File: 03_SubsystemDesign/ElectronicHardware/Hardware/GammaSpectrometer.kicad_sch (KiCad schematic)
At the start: 0 parts

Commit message: pcb design work in progress
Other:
- sheet AFE ports: added +5V0_A; removed +3V3_A, -3V3_A
- sheet Analog Power ports: added +5V0_A; removed -3V3_A
- sheet FPGA IO Banks 0-1 ports: added {CLK}; removed none
- note removed: "Add Signal Domain Color Coding (Optional but pro) Some teams: Use green for power Blue for high-speed Orange for control"
- note removed: "At 65 MSPS, 12-bit parallel bus: Are you using series termination? Is FPGA bank voltage matching DRVDD? Is IO standard LVTTL 3.3 V? Is timing margin analyzed? Even if handled in sub-sheets, the system sheet should imply interface class."
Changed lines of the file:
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@@
-		)
-	)
-	(text "Add Signal Domain Color Coding (Optional but pro)\nSome teams:\n\nUse green for power\nBlue for high-speed\nOrange for control"
-		(exclude_from_sim no)
-		(at 62.23 161.29 0)
-		(effects
-			(font
-				(size 1.27 1.27)
-			)
-		)
-	)
-	(text "At 65 MSPS, 12-bit parallel bus:\n\nAre you using series termination?\nIs FPGA bank voltage matching DRVDD?\nIs IO standard LVTTL 3.3 V?\nIs timing margin analyzed?\nEven if handled in sub-sheets, the system sheet should imply interface class."
-		(exclude_from_sim no)
-		(at 83.82 76.2 0)
-		(effects
-			(font
-				(size 1.27 1.27)
-			)
 		)
 	)
@@
 	)
 	(junction
-		(at 153.67 40.64)
-		(diameter 0)
-		(color 0 0 0 0)
-	)
-	(junction
 		(at 171.45 106.68)
 		(diameter 0)
@@
 	)
 	(junction
-		(at 156.21 38.1)
+		(at 102.87 99.06)
 		(diameter 0)
 		(color 0 0 0 0)
@@
 		(color 0 0 0 0)
 	)
-	(wire
-		(pts
-			(xy 105.41 38.1) (xy 156.21 38.1)
+	(junction
+		(at 144.78 125.73)
+		(diameter 0)
+		(color 0 0 0 0)
+	)
+	(wire
+		(pts
+			(xy 105.41 38.1) (xy 194.31 38.1)
 		)
 		(stroke
@@
 	(wire
 		(pts
-			(xy 92.71 99.06) (xy 105.41 99.06)
+			(xy 92.71 99.06) (xy 102.87 99.06)
 		)
 		(stroke
@@
 		)
 	)
+	(bus
+		(pts
+			(xy 144.78 153.67) (xy 173.99 153.67)
+		)
+		(stroke
+			(width 0)
+			(type default)
+		)
+	)
 	(wire
 		(pts
@@
 	(wire
 		(pts
-			(xy 194.31 40.64) (xy 153.67 40.64)
-		)
-		(stroke
-			(width 0)
-			(type default)
-		)
-	)
-	(wire
-		(pts
 			(xy 187.96 45.72) (xy 194.31 45.72)
 		)
@@
 	(wire
 		(pts
-			(xy 194.31 38.1) (xy 156.21 38.1)
+			(xy 153.67 45.72) (xy 153.67 35.56)
+		)
+		(stroke
+			(width 0)
+			(type default)
+		)
+	)
+	(wire
+		(pts
+			(xy 102.87 40.64) (xy 102.87 99.06)
 		)
 		(stroke
@@
 		)
 	)
+	(bus
+		(pts
+			(xy 144.78 125.73) (xy 144.78 153.67)
+		)
+		(stroke
+			(width 0)
+			(type default)
+		)
+	)
+	(wire
+		(pts
+			(xy 158.75 45.72) (xy 153.67 45.72)
+		)
+		(stroke
+			(width 0)
+			(type default)
+		)
+	)
 	(wire
 		(pts
@@
 	(wire
 		(pts
-			(xy 95.25 40.64) (xy 153.67 40.64)
-		)
-		(stroke
-			(width 0)
-			(type default)
-		)
-	)
-	(wire
-		(pts
 			(xy 187.96 52.07) (xy 194.31 52.07)
 		)
@@
 	(wire
 		(pts
-			(xy 156.21 38.1) (xy 156.21 45.72)
+			(xy 194.31 40.64) (xy 102.87 40.64)
+		)
+		(stroke
+			(width 0)
+			(type default)
+		)
+	)
+	(bus
+		(pts
+			(xy 144.78 120.65) (xy 144.78 125.73)
 		)
 		(stroke
@@
 		)
 	)
-	(wire
-		(pts
-			(xy 158.75 48.26) (xy 153.67 48.26)
-		)
-		(stroke
-			(width 0)
-			(type default)
-		)
-	)
 	(bus
 		(pts
@@
 	(bus
 		(pts
+			(xy 137.16 120.65) (xy 144.78 120.65)
+		)
+		(stroke
+			(width 0)
+			(type default)
+		)
+	)
+	(bus
+		(pts
 			(xy 153.67 148.59) (xy 173.99 148.59)
 		)
@@
 	(wire
 		(pts
+			(xy 95.25 35.56) (xy 153.67 35.56)
+		)
+		(stroke
+			(width 0)
+			(type default)
+		)
+	)
+	(wire
+		(pts
 			(xy 92.71 104.14) (xy 100.33 104.14)
 		)
@@
 	(wire
 		(pts
-			(xy 156.21 45.72) (xy 158.75 45.72)
-		)
-		(stroke
-			(width 0)
-			(type default)
-		)
-	)
-	(wire
-		(pts
 			(xy 205.74 140.97) (xy 219.71 140.97)
 		)
@@
 	(wire
 		(pts
+			(xy 102.87 99.06) (xy 105.41 99.06)
+		)
+		(stroke
+			(width 0)
+			(type default)
+		)
+	)
+	(wire
+		(pts
 			(xy 171.45 99.06) (xy 214.63 99.06)
 		)
@@
 		)
 	)
+	(bus
+		(pts
+			(xy 173.99 125.73) (xy 144.78 125.73)
+		)
+		(stroke
+			(width 0)
+			(type default)
+		)
+	)
 	(wire
 		(pts
 			(xy 135.89 53.34) (xy 158.75 53.34)
-		)
-		(stroke
-			(width 0)
-			(type default)
-		)
-	)
-	(wire
-		(pts
-			(xy 153.67 40.64) (xy 153.67 48.26)
 		)
 		(stroke
@@
 	)
 	(sheet
-		(at 69.85 35.56)
+		(at 69.85 33.02)
 		(size 25.4 7.62)
 		(exclude_from_sim no)
@@
 		)
 		(property "Sheetname" "Analog Power"
-			(at 69.85 34.8484 0)
+			(at 69.85 32.3084 0)
 			(show_name no)
 			(do_not_autoplace no)
@@
 		)
 		(property "Sheetfile" "AnalogPower.kicad_sch"
-			(at 69.85 43.7646 0)
+			(at 69.85 41.2246 0)
 			(show_name no)
 			(do_not_autoplace no)
@@
 			)
 		)
-		(pin "-3V3_A" output
-			(at 95.25 40.64 0)
-			(effects
-				(font
-					(size 1.27 1.27)
-				)
-				(justify right)
-			)
-		)
 		(pin "+3V3_A" output
 			(at 95.25 38.1 0)
+			(effects
+				(font
+					(size 1.27 1.27)
+				)
+				(justify right)
+			)
+		)
+		(pin "+5V0_A" output
+			(at 95.25 35.56 0)
 			(effects
 				(font
@@
 			)
 		)
-		(pin "SIPM_ADC_CH1_OTR" output
+		(pin "SIPM_ADC_CH1_OTR" input
 			(at 173.99 114.3 180)
+			(effects
+				(font
+					(size 1.27 1.27)
+				)
+				(justify left)
+			)
+		)
+		(pin "{CLK}" output
+			(at 173.99 125.73 180)
 			(effects
 				(font
@@
 	(sheet
 		(at 158.75 43.18)
-		(size 29.21 15.24)
+		(size 29.21 13.97)
 		(exclude_from_sim no)
 		(in_bom yes)
@@
 		)
 		(property "Sheetfile" "AFE.kicad_sch"
-			(at 158.75 59.0046 0)
+			(at 158.75 57.7346 0)
 			(show_name no)
 			(do_not_autoplace no)
@@
 			)
 		)
-		(pin "+3V3_A" input
+		(pin "+5V0_A" input
 			(at 158.75 45.72 180)
 			(effects
 				(font
-					(size 1.27 1.27)
-				)
-				(justify left)
-			)
-		)
-		(pin "-3V3_A" input
-			(at 158.75 48.26 180)
-			(effects
-				(font

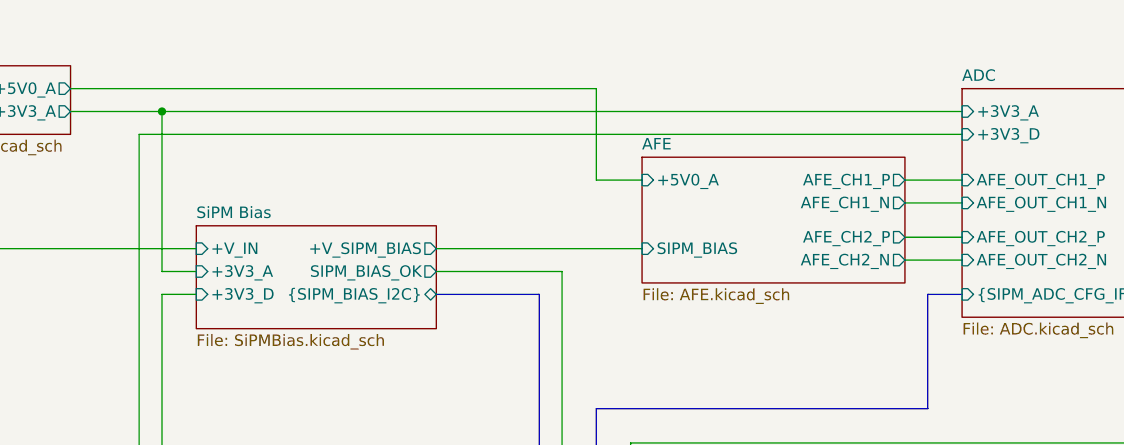
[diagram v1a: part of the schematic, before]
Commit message: improve CAD folder structure and PCB
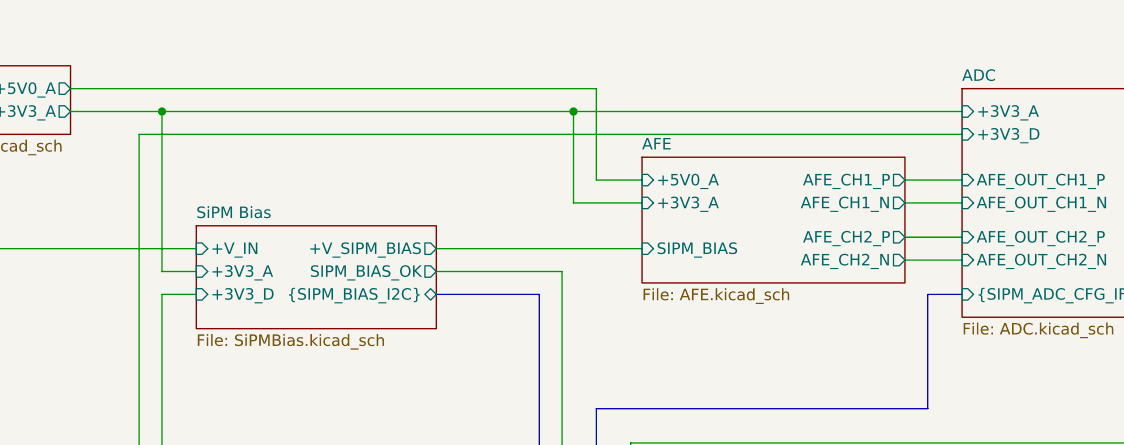
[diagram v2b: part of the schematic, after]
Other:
- sheet AFE ports: added +3V3_A; removed none
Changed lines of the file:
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@@
+	)
+	(junction
+		(at 151.13 38.1)
+		(diameter 0)
+		(color 0 0 0 0)
 	)
 	(junction
@@
 	(wire
 		(pts
-			(xy 105.41 38.1) (xy 194.31 38.1)
+			(xy 105.41 38.1) (xy 151.13 38.1)
+		)
+		(stroke
+			(width 0)
+			(type default)
+		)
+	)
+	(wire
+		(pts
+			(xy 158.75 48.26) (xy 151.13 48.26)
 		)
 		(stroke
@@
 	(wire
 		(pts
+			(xy 151.13 48.26) (xy 151.13 38.1)
+		)
+		(stroke
+			(width 0)
+			(type default)
+		)
+	)
+	(wire
+		(pts
 			(xy 173.99 138.43) (xy 171.45 138.43)
 		)
@@
 		(pts
 			(xy 242.57 74.93) (xy 157.48 74.93)
+		)
+		(stroke
+			(width 0)
+			(type default)
+		)
+	)
+	(wire
+		(pts
+			(xy 151.13 38.1) (xy 194.31 38.1)
 		)
 		(stroke
@@
 			(effects
 				(font
+					(size 1.27 1.27)
+				)
+				(justify left)
+			)
+		)
+		(pin "+3V3_A" input
+			(at 158.75 48.26 180)
+			(effects
+				(font
